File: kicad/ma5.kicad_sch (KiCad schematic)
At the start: 71 parts, among them K1 A2F1CSQ12VDC1.6, K2 CONTACTOR, K3 A2F1CSQ12VDC1.6, K4 A2F1CSQ12VDC1.6, K5 A2F1CSQ12VDC1.6, K6 CONTACTOR, K7 A2F1CSQ12VDC1.6, K8 A2F1CSQ12VDC1.6, K9 contactor, M1 alt, M2 starter, M3 #2 fuel pump, M4 #1 fuel pump, SW1 1-3, SW10 1-3, SW11 push-btn, SW12 2-10, SW13 2-10, SW14 1-3, SW17 1-3, SW20 START, SW3 2-10, SW5 1-3, SW9 2-10, U1 #1 coil pack, U3 LRD3-14, U4 REAR EFIS, U5 FRONT EFIS, U6 TRANSPONDER, U7 RADIO, U8 #2 coil pack

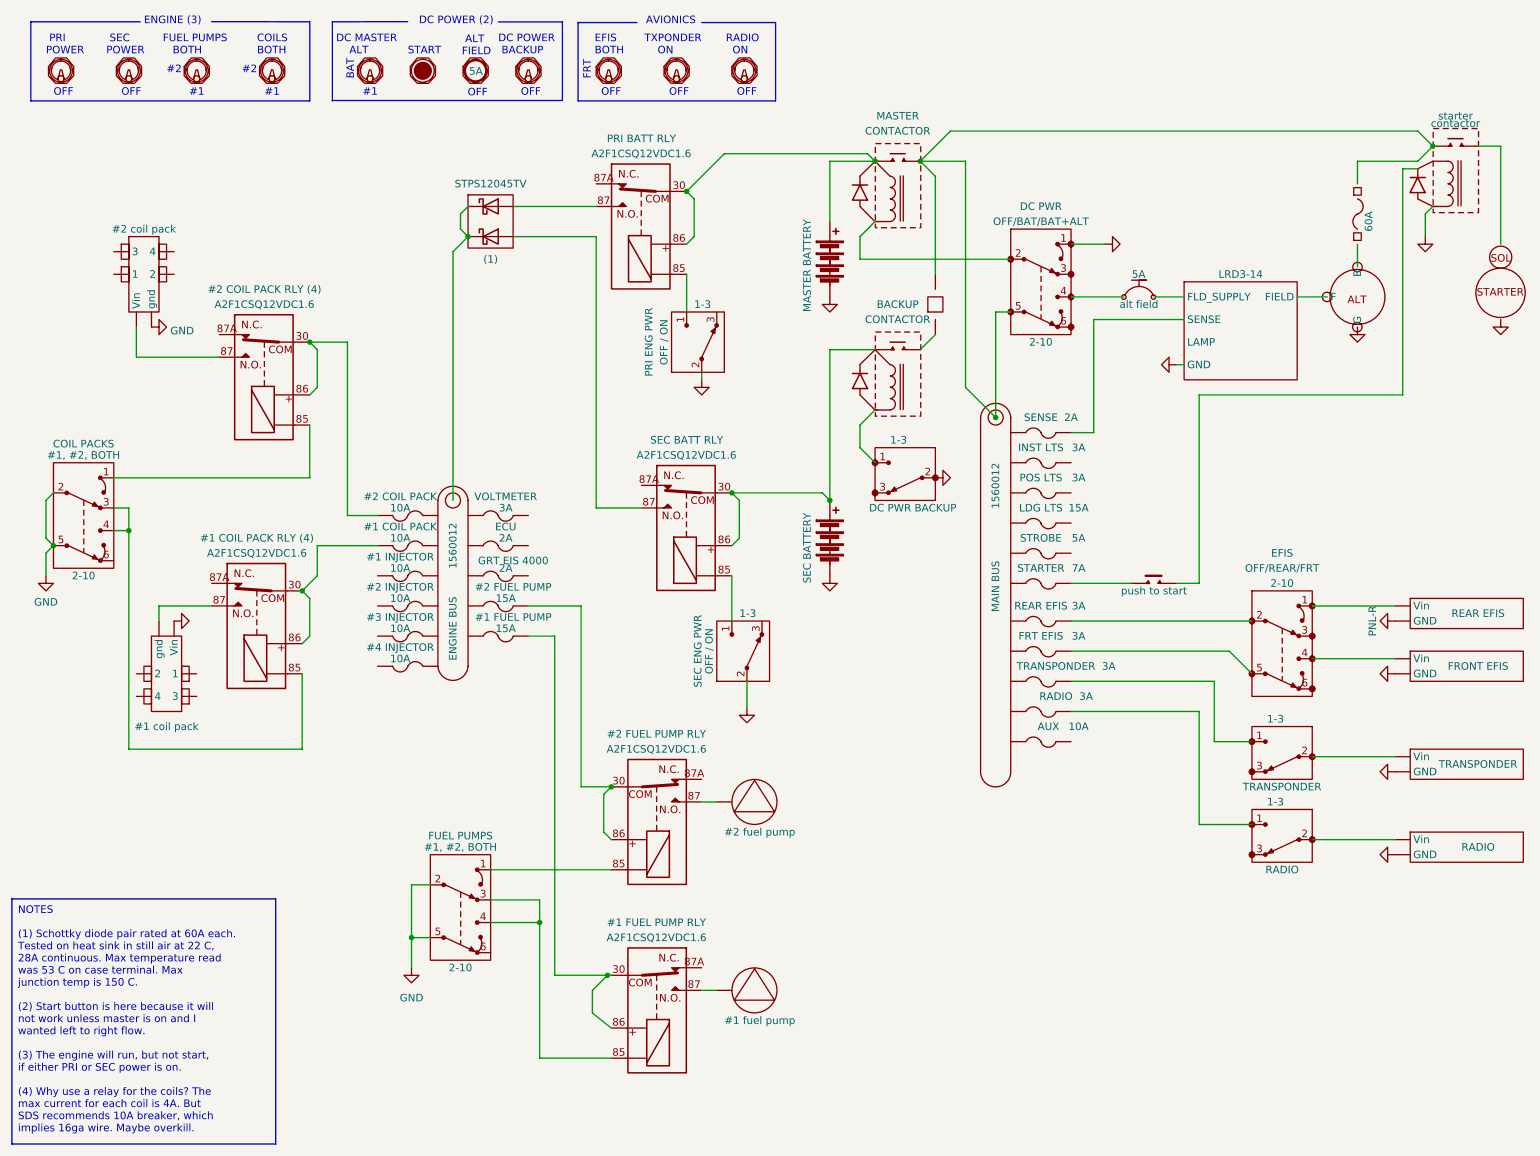
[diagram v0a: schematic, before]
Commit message: separate efis switches
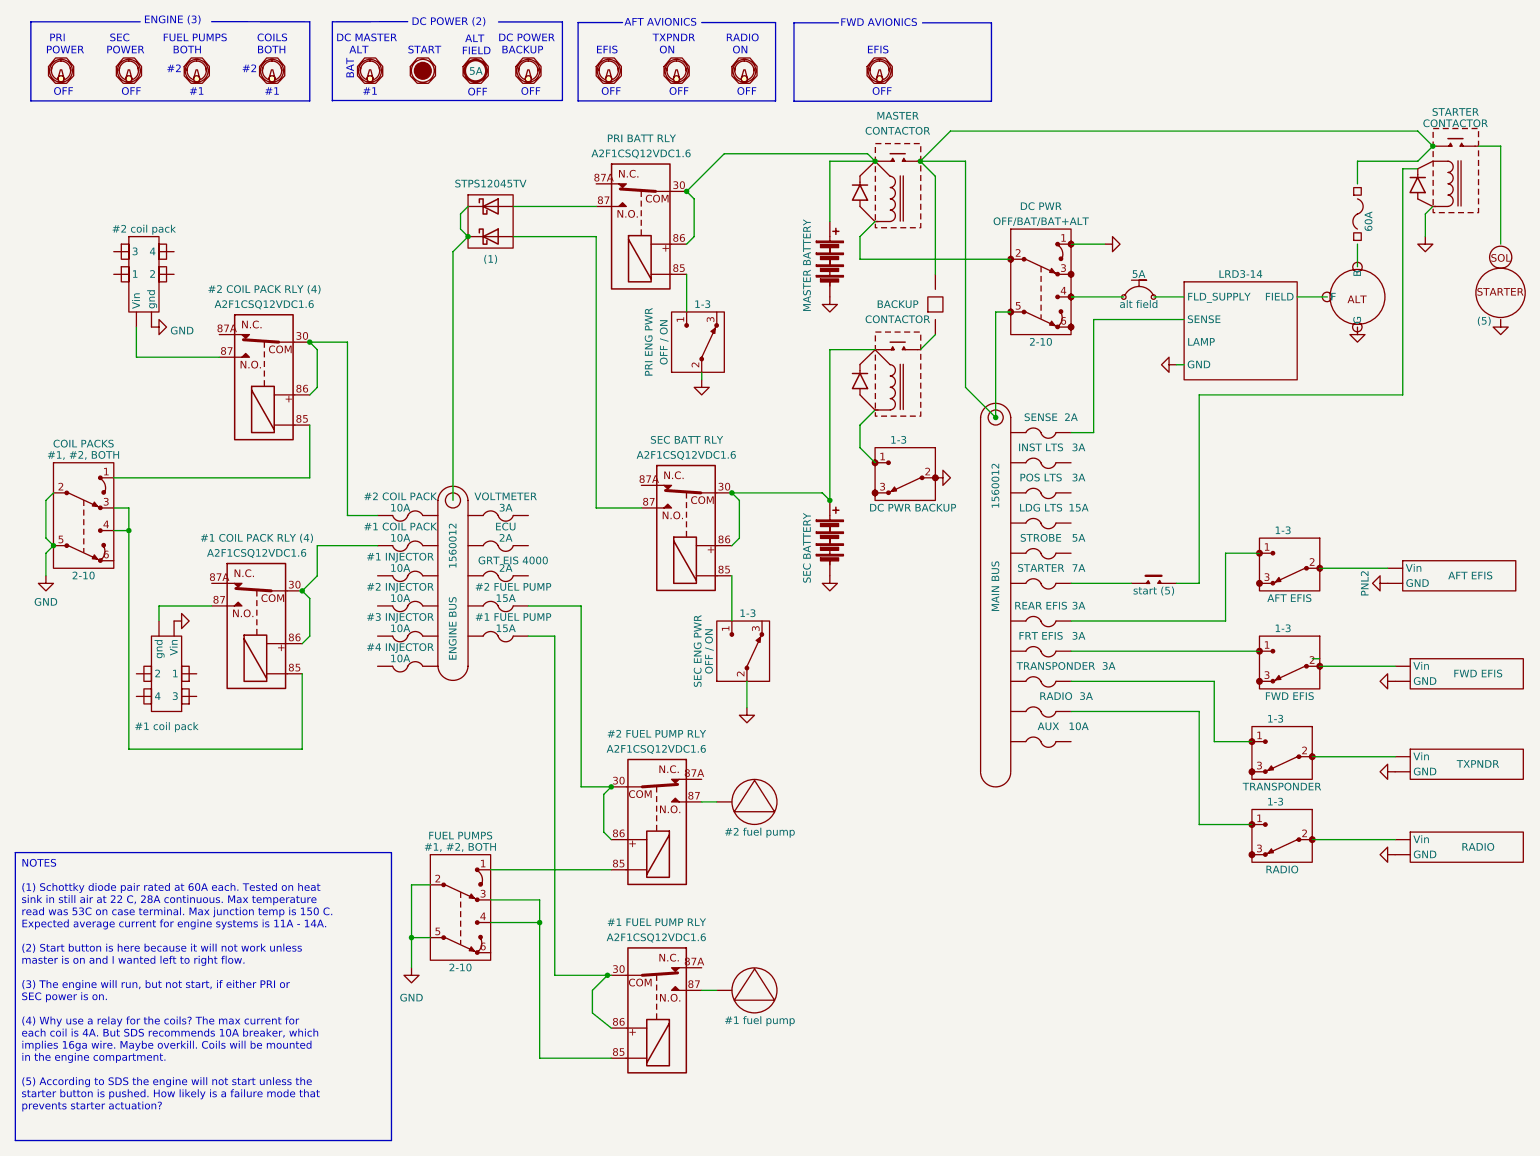
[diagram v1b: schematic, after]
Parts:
- removed SW12: 2-10, symbol ma5_:2-10
- added SW12, SW21: 1-3, symbol ma5_:1-3
- added SW22: ~, symbol ma5_:switch_graphic
- K9: value contactor -> CONTACTOR; Label starter -> STARTER
- M2: Note (none) -> (5)
- SW11: label push to start -> start (5)
- U4: value REAR EFIS -> AFT EFIS
- U5: value FRONT EFIS -> FWD EFIS
- U6: value TRANSPONDER -> TXPNDR
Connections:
- net at F4.: now also FB1.5 (5A)
- net at F12.: now also FB1.7 (5A)
- net at F21.: now also SW21.1
- net at F20.: now also SW12.1
- net at K9.: now also SW11.1
- net at CB1.: now also SW13.4; no longer U3. (SENSE)
- new net: SW12.2, U4. (Vin)
- new net: SW21.2, U5. (Vin)
- new net: M1. (G), U3. (SENSE)
- new net: CB1., U3. (SENSE)
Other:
- note added: "AFT AVIONICS"
- note added: "EFIS"
- note added: "FWD AVIONICS"
- note added: "TXPNDR ON"
- note removed: "AVIONICS"
- note removed: "EFIS BOTH"
- note removed: "FRT"
- note removed: "TXPONDER ON"

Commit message: AWG labels
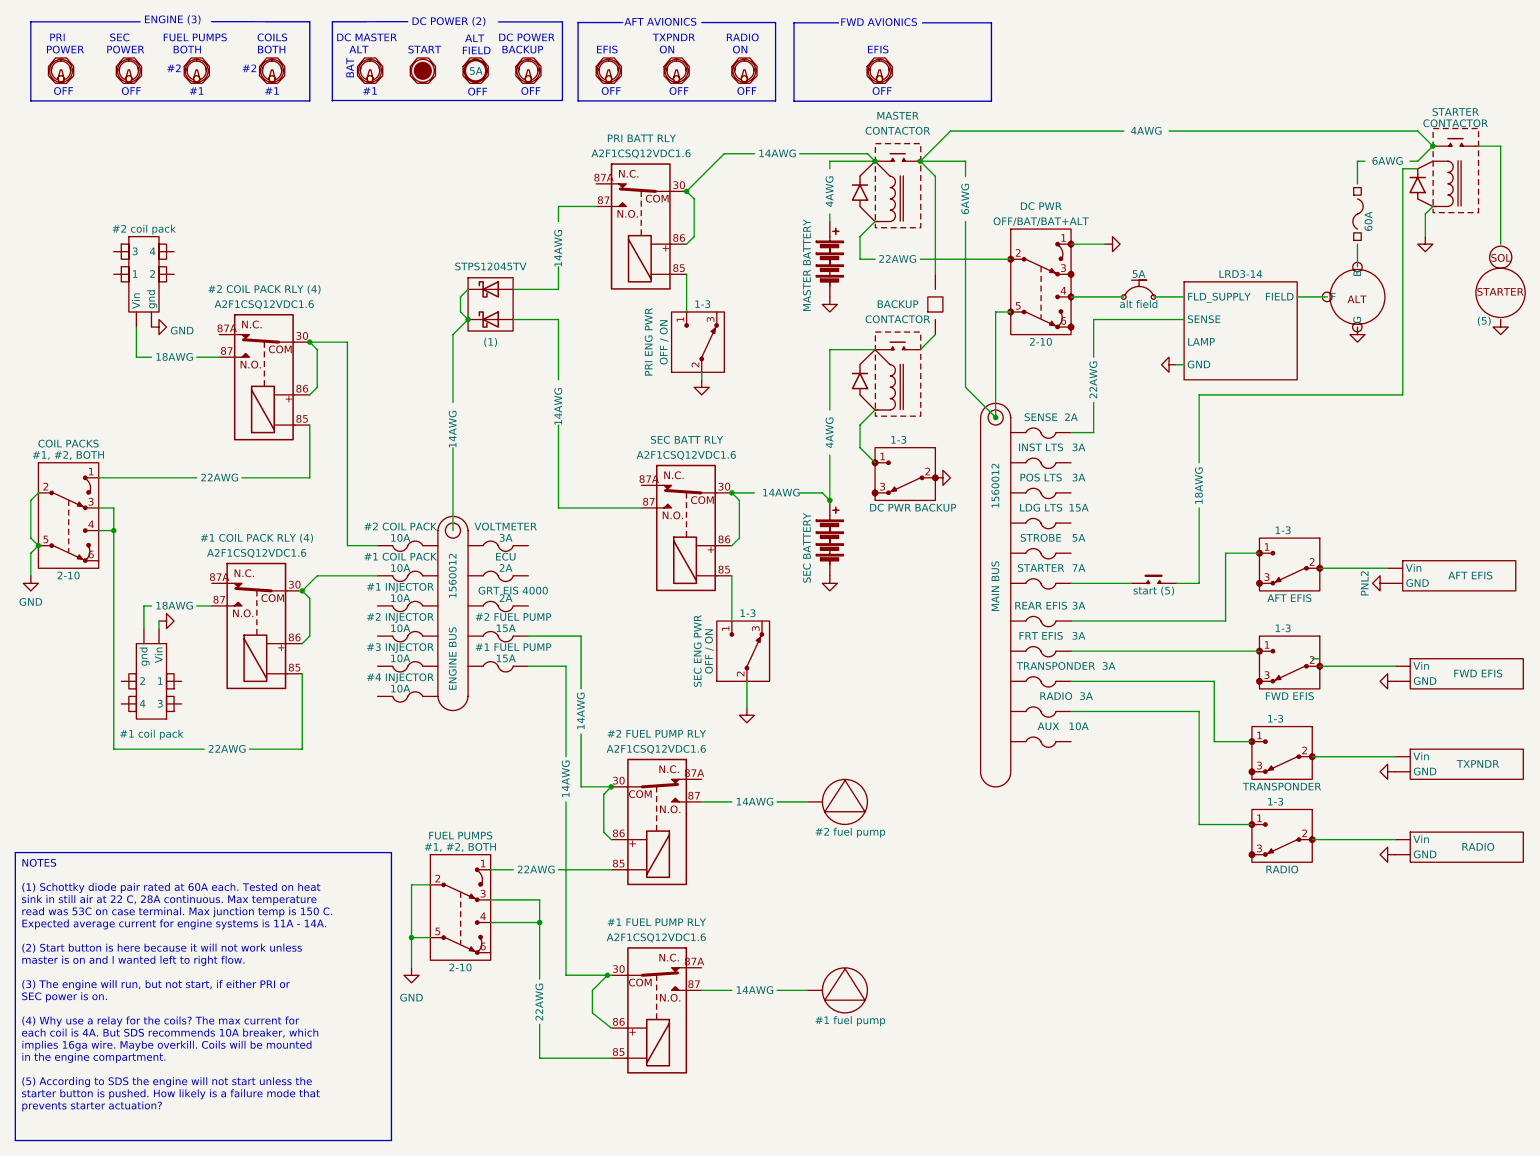
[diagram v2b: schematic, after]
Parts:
- added F25, F47, F48: 4AWG, symbol ma5_:4AWG
- added F26, F32: 6AWG, symbol ma5_:6AWG
- added F27, F28, F29, F30, F31, F36, F37, F38, F39: 14AWG, symbol ma5_:14AWG
- added F33, F34, F40, F41, F42, F43: 22AWG, symbol ma5_:22AWG
- added F35, F44, F46: 18AWG, symbol ma5_:18AWG
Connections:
- net at K5.30, K5.86: now also F30.; no longer BT1.1 (+), K6.1
- net at SW9.1: now also F43.; no longer K7.85
- net at SW9.3, SW9.4: now also F42.; no longer K8.85
- net at F4.: now also FB1.5 (5A)
- net at F12.: now also FB1.7 (5A)
- net at SW3.1: now also F41.; no longer K1.85
- net at SW3.3, SW3.4: now also F40.; no longer K3.85
- net at D1.1 (K), D1.4 (K): now also F31.; no longer FB1. (Vin)
- net at K4.30, K4.86: now also F29.; no longer BT2.1 (+), K2.1
- net at K2.2: now also F33.; no longer SW13.2
- net at M4.: now also F37.; no longer K3.87
- net at F1.: now also F26.; no longer M1. (G)
- net at U8.5 (Vin): now also F44.; no longer K7.87
- net at K3.30, K3.86: now also F38.; no longer F7.
- net at U1.6 (gnd): now also F46.; no longer K8.87
- net at M3.: now also F36.; no longer K1.87
- net at K4.87: now also F27.; no longer D1.2 (A)
- net at K5.87: now also F28.; no longer D1.3 (A)
- net at K9.: now also F35.
- net at SW11.1: now also F35.; no longer K9.
- net at K1.30, K1.86: now also F39.; no longer F6.
- net at F14.: now also F34.; no longer U3. (SENSE)
- net at CB1.: now also SW13.4; no longer U3. (SENSE)
- new net: F41., K1.85
- new net: BT1.1 (+), F30., F47.
- new net: F32., FB2. (Vin), SW13.5
- new net: F38., F7.
- new net: F31., FB1. (Vin)
- new net: F42., K8.85
- new net: F25., F3., F32., K2.3 (2)
- new net: F29., F48., K2.1
- new net: BT2.1 (+), F48.
- new net: F39., F6.
- new net: F1., M1. (G)
- new net: F40., K3.85
- new net: F37., K3.87
- new net: F43., K7.85
- new net: F44., K7.87
- new net: F33., SW13.2
- new net: F47., K6.1
- new net: F25., F26., K9.1
- new net: F34., U3. (SENSE)
- new net: D1.2 (A), F27.
- new net: D1.3 (A), F28.
- new net: F36., K1.87
- new net: F46., K8.87
- new net: M1. (G), U3. (SENSE)
- new net: CB1., U3. (SENSE)

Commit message: kicad schematic pdf
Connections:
- net at F4.: now also FB1.5 (5A)
- net at F12.: now also FB1.7 (5A)
- net at F1.: now also F26.; no longer M1. (G)
- net at F26.: now also F25., K9.1; no longer F1.
- net at K9.: now also F35.
- net at F35.: now also SW11.1; no longer K9.
- net at CB1.: now also SW13.4; no longer U3. (SENSE)
- new net: BT1.1 (+), F30., F47.
- new net: F29., F48., K2.1
- new net: F1., M1. (G)
- new net: M1. (G), U3. (SENSE)
- new net: CB1., U3. (SENSE)
